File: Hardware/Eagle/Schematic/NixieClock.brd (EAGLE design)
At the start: 160 x 100 mm, 4 parts

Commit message: Schematic progress
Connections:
- new net N$3: U$1.D4, U$2.P$14
- new net N$4: U$1.D2, U$2.P$11, U$3.P$11, U$4.P$11
- new net N$5: U$1.D3, U$2.P$12, U$3.P$12, U$4.P$12
- new net N$6: U$1.GND@3, U$2.P$8, U$3.P$8, U$4.P$8
- net N$2: now also U$2.P$10, U$3.P$10, U$4.P$10
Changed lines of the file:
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@@
 <contactref element="U$3" pad="P$16"/>
 <contactref element="U$4" pad="P$16"/>
-<wire x1="-13.97" y1="71.12" x2="135.89" y2="31.75" width="0" layer="19" extent="1-1"/>
+<contactref element="U$3" pad="P$10"/>
+<contactref element="U$4" pad="P$10"/>
+<contactref element="U$2" pad="P$10"/>
+<wire x1="-13.97" y1="55.88" x2="135.89" y2="31.75" width="0" layer="19" extent="1-1"/>
+<wire x1="-24.13" y1="55.88" x2="-13.97" y2="55.88" width="0" layer="19" extent="1-1"/>
+<wire x1="-13.97" y1="71.12" x2="-13.97" y2="55.88" width="0" layer="19" extent="1-1"/>
 <wire x1="-24.13" y1="71.12" x2="-13.97" y2="71.12" width="0" layer="19" extent="1-1"/>
-<wire x1="-40.64" y1="21.59" x2="-24.13" y2="71.12" width="0" layer="19" extent="1-1"/>
+<wire x1="-40.64" y1="21.59" x2="-24.13" y2="55.88" width="0" layer="19" extent="1-1"/>
+<wire x1="-40.64" y1="6.35" x2="-40.64" y2="21.59" width="0" layer="19" extent="1-1"/>
+</signal>
+<signal name="N$3">
+<contactref element="U$1" pad="D4"/>
+<contactref element="U$2" pad="P$14"/>
+<wire x1="-40.64" y1="16.51" x2="135.89" y2="57.15" width="0" layer="19" extent="1-1"/>
+</signal>
+<signal name="N$4">
+<contactref element="U$1" pad="D2"/>
+<contactref element="U$2" pad="P$11"/>
+<contactref element="U$3" pad="P$11"/>
+<contactref element="U$4" pad="P$11"/>
+<wire x1="-13.97" y1="58.42" x2="135.89" y2="62.23" width="0" layer="19" extent="1-1"/>
+<wire x1="-24.13" y1="58.42" x2="-13.97" y2="58.42" width="0" layer="19" extent="1-1"/>
+<wire x1="-40.64" y1="8.89" x2="-24.13" y2="58.42" width="0" layer="19" extent="1-1"/>
+</signal>
+<signal name="N$5">
+<contactref element="U$1" pad="D3"/>
+<contactref element="U$2" pad="P$12"/>
+<contactref element="U$3" pad="P$12"/>
+<contactref element="U$4" pad="P$12"/>
+<wire x1="-13.97" y1="60.96" x2="135.89" y2="59.69" width="0" layer="19" extent="1-1"/>
+<wire x1="-24.13" y1="60.96" x2="-13.97" y2="60.96" width="0" layer="19" extent="1-1"/>
+<wire x1="-40.64" y1="11.43" x2="-24.13" y2="60.96" width="0" layer="19" extent="1-1"/>
+</signal>
+<signal name="N$6">
+<contactref element="U$1" pad="GND@3"/>
+<contactref element="U$2" pad="P$8"/>
+<contactref element="U$3" pad="P$8"/>
+<contactref element="U$4" pad="P$8"/>
+<wire x1="-21.59" y1="53.34" x2="135.89" y2="34.29" width="0" layer="19" extent="1-1"/>
+<wire x1="-31.75" y1="53.34" x2="-21.59" y2="53.34" width="0" layer="19" extent="1-1"/>
+<wire x1="-48.26" y1="3.81" x2="-31.75" y2="53.34" width="0" layer="19" extent="1-1"/>
 </signal>
 </signals>

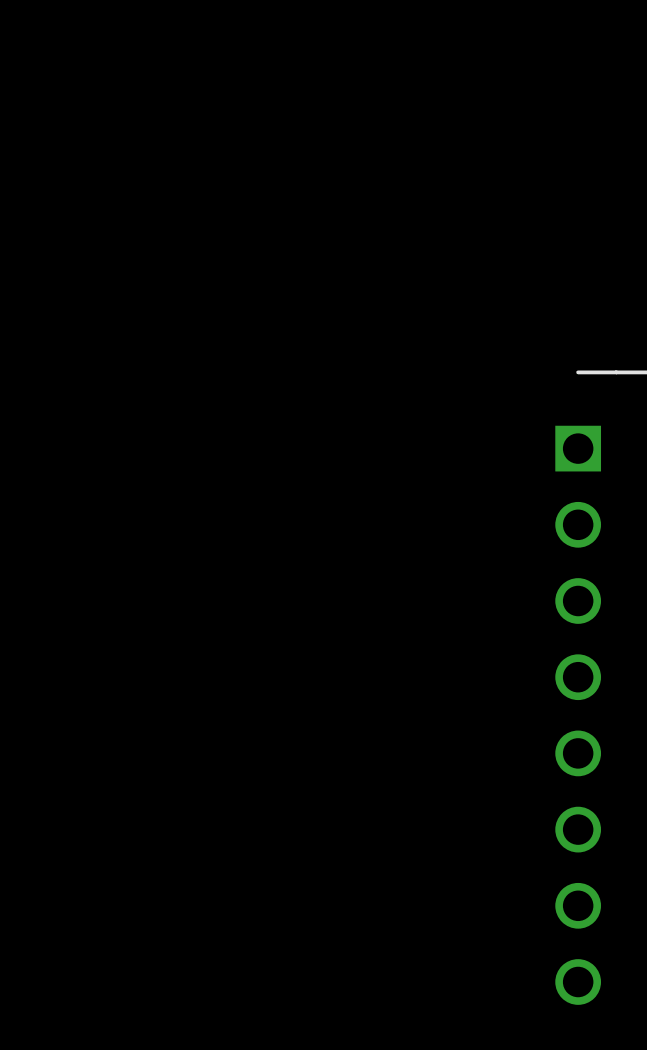
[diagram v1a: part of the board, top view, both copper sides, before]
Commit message: Schematic progress.. made nixie tube driver chip lib
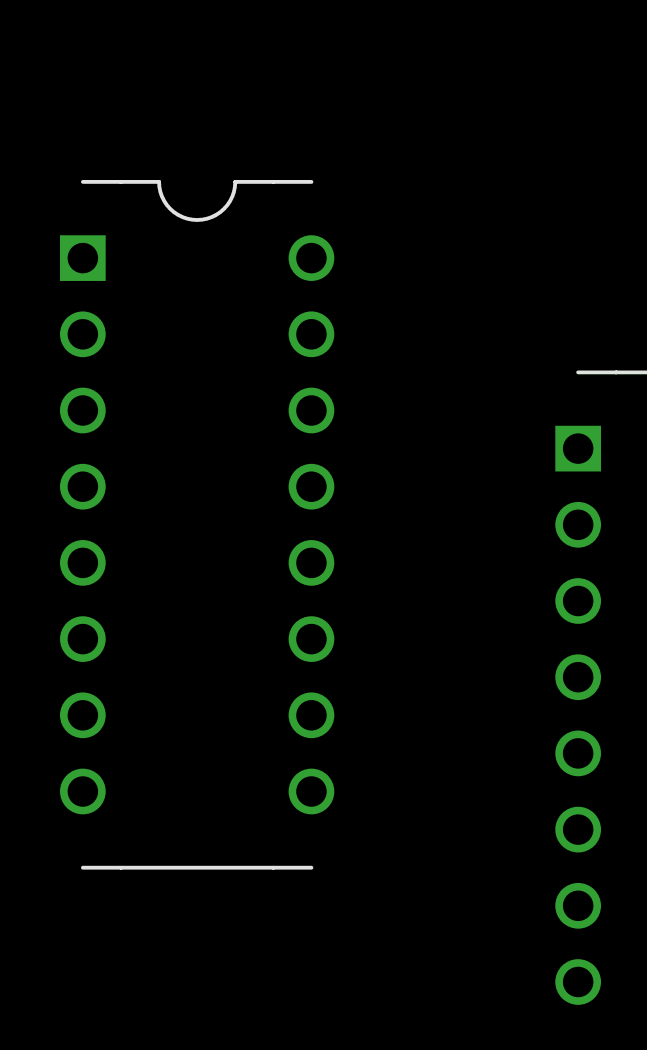
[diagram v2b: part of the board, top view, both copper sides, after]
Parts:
- added U$5: DM5441ADIP-16, DM5441A:DIP-16
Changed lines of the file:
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@@
 <attribute name="PRICE" value="None" x="0" y="0" size="1.778" layer="27" display="off"/>
+</element>
+<element name="U$5" library="DM5441A" package="DIP-16" value="DM5441ADIP-16" x="-60.96" y="19.05" smashed="yes">
+<attribute name="AVAILABILITY" value="Unavailable" x="-60.96" y="19.05" size="1.778" layer="27" display="off"/>
+<attribute name="DESCRIPTION" value=" Shift Register Single 8 Bit Serial To Serial Parallel 16 Pin Plastic DIP Tube " x="-60.96" y="19.05" size="1.778" layer="27" display="off"/>
+<attribute name="MF" value="Texas Instruments" x="-60.96" y="19.05" size="1.778" layer="27" display="off"/>
+<attribute name="MP" value="SN74HC595N" x="-60.96" y="19.05" size="1.778" layer="27" display="off"/>
+<attribute name="PACKAGE" value="PDIP-16 Texas Instruments" x="-60.96" y="19.05" size="1.778" layer="27" display="off"/>
+<attribute name="PRICE" value="None" x="-60.96" y="19.05" size="1.778" layer="27" display="off"/>
 </element>
 </elements>

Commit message: Schematic Progress
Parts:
- added U$10, U$6, U$7, U$8, U$9: DM5441ADIP-16, DM5441A:DIP-16
- moved U$3 89.2 mm to (71.1, 69.8), turned to 90 degrees
- moved U$2 58.5 mm to (-41.9, 71.1), turned to 90 degrees
- moved U$4 44.1 mm to (15.2, 71.1), turned to 90 degrees
- moved U$5 34.5 mm to (-57.1, 53.3), turned to 90 degrees
- turned U$1 to 90 degrees
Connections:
- new net N$8: U$1.3V3@0, U$10.P$5, U$5.P$5, U$6.P$5, U$7.P$5, U$8.P$5, U$9.P$5
- net N$1: now also U$10.P$12, U$5.P$12, U$6.P$12, U$7.P$12, U$8.P$12, U$9.P$12
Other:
- board size 160 x 100 mm -> 256.5 x 112.7 mm

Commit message: Schematic progress
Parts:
- moved U$4 14.0 mm to (15.2, 57.1)
- moved U$10 12.7 mm to (85.1, 40.6)
- moved U$2 12.7 mm to (-41.9, 58.4)
- moved U$5 12.7 mm to (-57.1, 40.6)
- moved U$6 12.7 mm to (-26.7, 40.6)
- moved U$7 12.7 mm to (1.27, 40.6)
- moved U$8 12.7 mm to (31.8, 40.6)
- moved U$9 12.7 mm to (58.4, 40.6)
- moved U$3 12.7 mm to (71.1, 57.1)
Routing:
- net N$2: track 0.00 -> 203.0 mm
- net N$6: track 0.00 -> 180.5 mm
- net N$3: track 0.00 -> 168.5 mm
- net N$5: track 0.00 -> 168.1 mm
- net N$4: track 0.00 -> 157.8 mm

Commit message: Schematic Progress
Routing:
- net N$8: track 0.00 -> 195.9 mm
- net N$1: track 0.00 -> 156.7 mm, vias 0 -> 2
- net N$4: track 157.8 -> 160.9 mm, vias 0 -> 1
- net N$5: track 168.1 -> 169.1 mm
- net N$2: track 203.0 -> 204.1 mm
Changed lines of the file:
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@@
 <layer number="43" name="vRestrict" color="2" fill="10" visible="yes" active="yes"/>
 <layer number="44" name="Drills" color="7" fill="1" visible="no" active="yes"/>
-<layer number="45" name="Holes" color="7" fill="1" visible="no" active="yes"/>
+<layer number="45" name="Holes" color="7" fill="1" visible="yes" active="yes"/>
 <layer number="46" name="Milling" color="3" fill="1" visible="no" active="yes"/>
 <layer number="47" name="Measures" color="7" fill="1" visible="no" active="yes"/>
@@
 <contactref element="U$9" pad="P$12"/>
 <contactref element="U$10" pad="P$12"/>
-<wire x1="86.36" y1="44.45" x2="129.54" y2="38.1" width="0" layer="19" extent="1-1"/>
-<wire x1="69.85" y1="60.96" x2="86.36" y2="44.45" width="0" layer="19" extent="1-1"/>
-<wire x1="59.69" y1="44.45" x2="69.85" y2="60.96" width="0" layer="19" extent="1-1"/>
-<wire x1="33.02" y1="44.45" x2="59.69" y2="44.45" width="0" layer="19" extent="1-1"/>
-<wire x1="13.97" y1="60.96" x2="33.02" y2="44.45" width="0" layer="19" extent="1-1"/>
-<wire x1="2.54" y1="44.45" x2="13.97" y2="60.96" width="0" layer="19" extent="1-1"/>
+<wire x1="129.54" y1="38.1" x2="129.54" y2="40.64" width="0.1524" layer="1"/>
+<wire x1="129.54" y1="40.64" x2="127" y2="43.18" width="0.1524" layer="1"/>
+<wire x1="127" y1="43.18" x2="87.63" y2="43.18" width="0.1524" layer="1"/>
+<wire x1="87.63" y1="43.18" x2="86.36" y2="44.45" width="0.1524" layer="1"/>
+<wire x1="86.36" y1="44.45" x2="86.36" y2="49.53" width="0.1524" layer="16"/>
+<wire x1="80.3148" y1="55.5752" x2="75.2348" y2="55.5752" width="0.1524" layer="16"/>
+<wire x1="86.36" y1="49.53" x2="80.3148" y2="55.5752" width="0.1524" layer="16"/>
+<wire x1="69.85" y1="60.96" x2="75.2348" y2="55.5752" width="0.1524" layer="16"/>
+<wire x1="69.85" y1="60.96" x2="68.58" y2="59.69" width="0.1524" layer="16"/>
+<wire x1="68.58" y1="59.69" x2="63.5" y2="59.69" width="0.1524" layer="16"/>
+<wire x1="63.5" y1="59.69" x2="59.69" y2="55.88" width="0.1524" layer="16"/>
+<wire x1="59.69" y1="55.88" x2="59.69" y2="44.45" width="0.1524" layer="16"/>
+<wire x1="59.69" y1="44.45" x2="58.42" y2="43.18" width="0.1524" layer="16"/>
+<wire x1="58.42" y1="43.18" x2="34.29" y2="43.18" width="0.1524" layer="16"/>
+<wire x1="34.29" y1="43.18" x2="33.02" y2="44.45" width="0.1524" layer="16"/>
+<wire x1="33.02" y1="44.45" x2="26.67" y2="50.8" width="0.1524" layer="16"/>
+<wire x1="26.67" y1="50.8" x2="26.67" y2="60.96" width="0.1524" layer="16"/>
+<via x="26.67" y="60.96" extent="1-16" drill="0.35"/>
+<wire x1="13.97" y1="60.96" x2="12.7" y2="62.23" width="0.1524" layer="16"/>
+<wire x1="12.7" y1="62.23" x2="3.81" y2="62.23" width="0.1524" layer="16"/>
+<wire x1="3.81" y1="62.23" x2="2.54" y2="60.96" width="0.1524" layer="16"/>
+<via x="2.54" y="60.96" extent="1-16" drill="0.35"/>
+<wire x1="13.97" y1="60.96" x2="26.67" y2="60.96" width="0" layer="19" extent="1-1"/>
+<wire x1="2.54" y1="44.45" x2="2.54" y2="60.96" width="0" layer="19" extent="1-1"/>
 <wire x1="-25.4" y1="44.45" x2="2.54" y2="44.45" width="0" layer="19" extent="1-1"/>
 <wire x1="-43.18" y1="62.23" x2="-25.4" y2="44.45" width="0" layer="19" extent="1-1"/>
@@
 <wire x1="-38.1" y1="64.77" x2="-48.26" y2="64.77" width="0.1524" layer="1"/>
 <wire x1="-48.26" y1="64.77" x2="-50.8" y2="62.23" width="0.1524" layer="1"/>
-<wire x1="6.35" y1="60.96" x2="7.62" y2="62.23" width="0.1524" layer="1"/>
-<wire x1="7.62" y1="62.23" x2="20.32" y2="62.23" width="0.1524" layer="1"/>
-<wire x1="20.32" y1="62.23" x2="21.59" y2="60.96" width="0.1524" layer="1"/>
+<wire x1="6.35" y1="60.96" x2="8.89" y2="58.42" width="0.1524" layer="1"/>
+<wire x1="21.59" y1="60.96" x2="19.05" y2="58.42" width="0.1524" layer="1"/>
+<wire x1="19.05" y1="58.42" x2="8.89" y2="58.42" width="0.1524" layer="1"/>
 </signal>
 <signal name="N$3">
@@
 <wire x1="25.401325" y1="55.878675" x2="86.361325" y2="55.878675" width="0.1524" layer="1"/>
 <wire x1="25.401325" y1="55.878675" x2="24.13" y2="57.15" width="0.1524" layer="1"/>
-<wire x1="24.13" y1="57.15" x2="5.08" y2="57.15" width="0.1524" layer="1"/>
-<wire x1="5.08" y1="57.15" x2="-40.64" y2="57.15" width="0.1524" layer="1"/>
+<wire x1="24.13" y1="57.15" x2="-40.64" y2="57.15" width="0.1524" layer="1"/>
 <wire x1="-40.64" y1="57.15" x2="-45.72" y2="62.23" width="0.1524" layer="1"/>
 <wire x1="86.361325" y1="55.878675" x2="87.7822" y2="54.4578" width="0.1524" layer="1"/>
@@
 <wire x1="111.76" y1="60.96" x2="106.68" y2="55.88" width="0.1524" layer="1"/>
 <wire x1="106.68" y1="55.88" x2="88.9" y2="55.88" width="0.1524" layer="1"/>
-<wire x1="88.9" y1="55.88" x2="87.63" y2="57.15" width="0.1524" layer="1"/>
-<wire x1="87.63" y1="57.15" x2="78.74" y2="57.15" width="0.1524" layer="1"/>
-<wire x1="78.74" y1="57.15" x2="74.93" y2="60.96" width="0.1524" layer="1"/>
-<wire x1="74.93" y1="60.96" x2="73.66" y2="62.23" width="0.1524" layer="16"/>
-<wire x1="73.66" y1="62.23" x2="20.32" y2="62.23" width="0.1524" layer="16"/>
-<wire x1="20.32" y1="62.23" x2="19.05" y2="60.96" width="0.1524" layer="16"/>
-<wire x1="19.05" y1="60.96" x2="16.51" y2="58.42" width="0.1524" layer="16"/>
-<wire x1="-38.1" y1="62.23" x2="-34.29" y2="58.42" width="0.1524" layer="16"/>
-<wire x1="16.51" y1="58.42" x2="-34.29" y2="58.42" width="0.1524" layer="16"/>
+<wire x1="88.9" y1="55.88" x2="86.36" y2="58.42" width="0.1524" layer="1"/>
+<wire x1="86.36" y1="58.42" x2="77.47" y2="58.42" width="0.1524" layer="1"/>
+<wire x1="77.47" y1="58.42" x2="74.93" y2="60.96" width="0.1524" layer="1"/>
+<wire x1="74.93" y1="60.96" x2="68.58" y2="67.31" width="0.1524" layer="16"/>
+<wire x1="68.58" y1="67.31" x2="45.72" y2="67.31" width="0.1524" layer="16"/>
+<wire x1="19.05" y1="60.96" x2="17.78" y2="59.69" width="0.1524" layer="16"/>
+<wire x1="-38.1" y1="62.23" x2="-35.56" y2="59.69" width="0.1524" layer="16"/>
+<wire x1="17.78" y1="59.69" x2="-35.56" y2="59.69" width="0.1524" layer="16"/>
+<via x="45.72" y="67.31" extent="1-16" drill="0.35"/>
+<wire x1="45.72" y1="67.31" x2="25.4" y2="67.31" width="0.1524" layer="1"/>
+<wire x1="25.4" y1="67.31" x2="19.05" y2="60.96" width="0.1524" layer="1"/>
 </signal>
 <signal name="N$5">
@@
 <contactref element="U$4" pad="P$12"/>
 <wire x1="114.3" y1="60.96" x2="104.14" y2="50.8" width="0.1524" layer="16"/>
-<wire x1="104.14" y1="50.8" x2="86.36" y2="50.8" width="0.1524" layer="16"/>
-<wire x1="86.36" y1="50.8" x2="81.28" y2="55.88" width="0.1524" layer="16"/>
-<wire x1="81.28" y1="55.88" x2="77.47" y2="55.88" width="0.1524" layer="16"/>
-<wire x1="77.47" y1="55.88" x2="72.39" y2="60.96" width="0.1524" layer="16"/>
-<wire x1="72.39" y1="60.96" x2="69.85" y2="63.5" width="0.1524" layer="16"/>
-<wire x1="19.05" y1="63.5" x2="16.51" y2="60.96" width="0.1524" layer="16"/>
-<wire x1="69.85" y1="63.5" x2="19.05" y2="63.5" width="0.1524" layer="16"/>
-<wire x1="16.51" y1="60.96" x2="15.24" y2="59.69" width="0.1524" layer="16"/>
+<wire x1="104.14" y1="50.8" x2="87.63" y2="50.8" width="0.1524" layer="16"/>
+<wire x1="87.63" y1="50.8" x2="81.28" y2="57.15" width="0.1524" layer="16"/>
+<wire x1="81.28" y1="57.15" x2="76.2" y2="57.15" width="0.1524" layer="16"/>
+<wire x1="76.2" y1="57.15" x2="72.39" y2="60.96" width="0.1524" layer="16"/>
+<wire x1="72.39" y1="60.96" x2="67.31" y2="66.04" width="0.1524" layer="16"/>
+<wire x1="21.59" y1="66.04" x2="16.51" y2="60.96" width="0.1524" layer="16"/>
+<wire x1="67.31" y1="66.04" x2="21.59" y2="66.04" width="0.1524" layer="16"/>
 <wire x1="-40.64" y1="62.23" x2="-39.37" y2="63.5" width="0.1524" layer="16"/>
-<wire x1="-31.75" y1="63.5" x2="-39.37" y2="63.5" width="0.1524" layer="16"/>
-<wire x1="-27.94" y1="59.69" x2="-31.75" y2="63.5" width="0.1524" layer="16"/>
-<wire x1="15.24" y1="59.69" x2="-27.94" y2="59.69" width="0.1524" layer="16"/>
+<wire x1="16.51" y1="60.96" x2="13.97" y2="63.5" width="0.1524" layer="16"/>
+<wire x1="13.97" y1="63.5" x2="-39.37" y2="63.5" width="0.1524" layer="16"/>
 </signal>
 <signal name="N$6">
@@
 <contactref element="U$6" pad="P$5"/>
 <contactref element="U$5" pad="P$5"/>
-<wire x1="86.36" y1="36.83" x2="132.08" y2="38.1" width="0" layer="19" extent="1-1"/>
-<wire x1="59.69" y1="36.83" x2="86.36" y2="36.83" width="0" layer="19" extent="1-1"/>
-<wire x1="33.02" y1="36.83" x2="59.69" y2="36.83" width="0" layer="19" extent="1-1"/>
-<wire x1="2.54" y1="36.83" x2="33.02" y2="36.83" width="0" layer="19" extent="1-1"/>
-<wire x1="-25.4" y1="36.83" x2="2.54" y2="36.83" width="0" layer="19" extent="1-1"/>
-<wire x1="-55.88" y1="36.83" x2="-25.4" y2="36.83" width="0" layer="19" extent="1-1"/>
+<wire x1="132.08" y1="38.1" x2="128.27" y2="34.29" width="0.1524" layer="1"/>
+<wire x1="128.27" y1="34.29" x2="88.9" y2="34.29" width="0.1524" layer="1"/>
+<wire x1="88.9" y1="34.29" x2="86.36" y2="36.83" width="0.1524" layer="1"/>
+<wire x1="86.36" y1="36.83" x2="85.09" y2="38.1" width="0.1524" layer="1"/>
+<wire x1="85.09" y1="38.1" x2="60.96" y2="38.1" width="0.1524" layer="1"/>
+<wire x1="60.96" y1="38.1" x2="59.69" y2="36.83" width="0.1524" layer="1"/>
+<wire x1="59.69" y1="36.83" x2="58.42" y2="38.1" width="0.1524" layer="1"/>
+<wire x1="58.42" y1="38.1" x2="34.29" y2="38.1" width="0.1524" layer="1"/>
+<wire x1="34.29" y1="38.1" x2="33.02" y2="36.83" width="0.1524" layer="1"/>
+<wire x1="33.02" y1="36.83" x2="31.75" y2="38.1" width="0.1524" layer="1"/>
+<wire x1="31.75" y1="38.1" x2="3.81" y2="38.1" width="0.1524" layer="1"/>
+<wire x1="3.81" y1="38.1" x2="2.54" y2="36.83" width="0.1524" layer="1"/>
+<wire x1="2.54" y1="36.83" x2="1.27" y2="38.1" width="0.1524" layer="1"/>
+<wire x1="1.27" y1="38.1" x2="-24.13" y2="38.1" width="0.1524" layer="1"/>
+<wire x1="-24.13" y1="38.1" x2="-25.4" y2="36.83" width="0.1524" layer="1"/>
+<wire x1="-25.4" y1="36.83" x2="-26.67" y2="38.1" width="0.1524" layer="1"/>
+<wire x1="-26.67" y1="38.1" x2="-54.61" y2="38.1" width="0.1524" layer="1"/>
+<wire x1="-54.61" y1="38.1" x2="-55.88" y2="36.83" width="0.1524" layer="1"/>
 </signal>
 </signals>
